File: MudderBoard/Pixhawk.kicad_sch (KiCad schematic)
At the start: 18 parts, among them U1 TPS566242DRLR, U2 LP38691DTX-3.3/NOPB

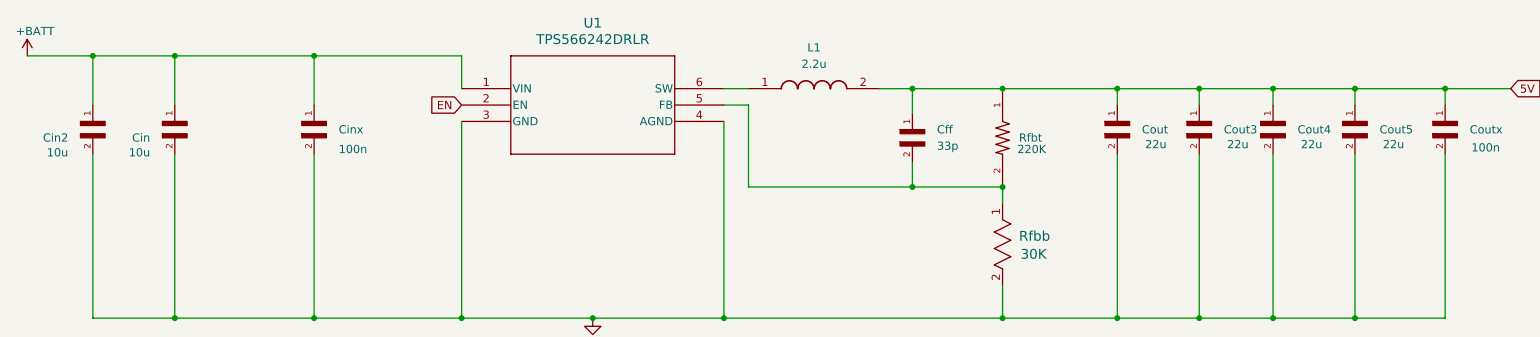
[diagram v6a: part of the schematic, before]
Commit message: Imported footprints to layout
Colin - Make note of these

C30,C32 are generic 0805 caps
L4,L5 are basic insuctors, will need to change when we figure this situation out!

U8,U9 changed to same boost IC as Lidar - these are the same right?
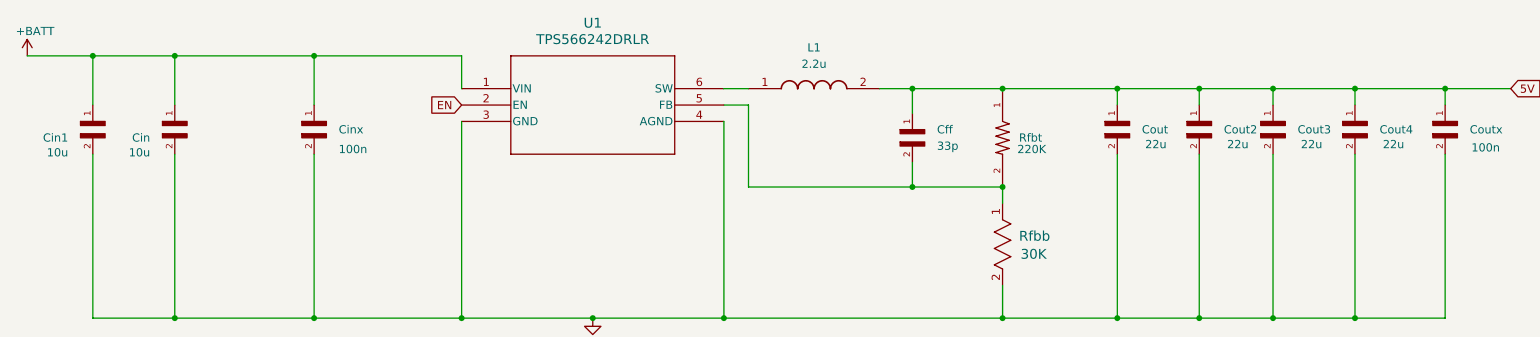
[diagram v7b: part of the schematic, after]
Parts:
- renumbered Cin2 to Cin1, Cout3 to Cout2, Cout4 to Cout3, Cout5 to Cout4
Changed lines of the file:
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@@
 			(project "MudderBoard"
 				(path "/cdf98bf7-80ce-4b13-b655-e6c7c589c122/0627c6a6-a63c-4c7b-88fc-6e03d8d4f91c"
-					(reference "L1")
+					(reference "L2")
 					(unit 1)
 				)
@@
 			(project "MudderBoard"
 				(path "/cdf98bf7-80ce-4b13-b655-e6c7c589c122/0627c6a6-a63c-4c7b-88fc-6e03d8d4f91c"
-					(reference "Cout2")
+					(reference "Cout1")
 					(unit 1)
 				)
@@
 		(on_board yes)
 		(dnp no)
-		(property "Reference" "Cout4"
+		(property "Reference" "Cout3"
 			(at 236.22 50.7999 90)
 			(effects
@@
 			(project "MudderBoard"
 				(path "/cdf98bf7-80ce-4b13-b655-e6c7c589c122/0627c6a6-a63c-4c7b-88fc-6e03d8d4f91c"
-					(reference "Cout4")
+					(reference "Cout3")
 					(unit 1)
 				)
@@
 			(project "MudderBoard"
 				(path "/cdf98bf7-80ce-4b13-b655-e6c7c589c122/0627c6a6-a63c-4c7b-88fc-6e03d8d4f91c"
-					(reference "Rfbb2")
+					(reference "Rfbb1")
 					(unit 1)
 				)
@@
 			(project "MudderBoard"
 				(path "/cdf98bf7-80ce-4b13-b655-e6c7c589c122/0627c6a6-a63c-4c7b-88fc-6e03d8d4f91c"
-					(reference "#PWR0104")
+					(reference "#PWR010")
 					(unit 1)
 				)
@@
 			(project "MudderBoard"
 				(path "/cdf98bf7-80ce-4b13-b655-e6c7c589c122/0627c6a6-a63c-4c7b-88fc-6e03d8d4f91c"
-					(reference "#PWR0101")
+					(reference "#PWR08")
 					(unit 1)
 				)
@@
 			(project "MudderBoard"
 				(path "/cdf98bf7-80ce-4b13-b655-e6c7c589c122/0627c6a6-a63c-4c7b-88fc-6e03d8d4f91c"
-					(reference "Cin3")
+					(reference "Cin2")
 					(unit 1)
 				)
@@
 			(project "MudderBoard"
 				(path "/cdf98bf7-80ce-4b13-b655-e6c7c589c122/0627c6a6-a63c-4c7b-88fc-6e03d8d4f91c"
-					(reference "U2")
+					(reference "U3")
 					(unit 1)
 				)
@@
 			(project "MudderBoard"
 				(path "/cdf98bf7-80ce-4b13-b655-e6c7c589c122/0627c6a6-a63c-4c7b-88fc-6e03d8d4f91c"
-					(reference "#PWR0103")
+					(reference "#PWR06")
 					(unit 1)
 				)
@@
 		(on_board yes)
 		(dnp no)
-		(property "Reference" "Cin2"
+		(property "Reference" "Cin1"
 			(at 45.72 52.0701 90)
 			(effects
@@
 			(project "MudderBoard"
 				(path "/cdf98bf7-80ce-4b13-b655-e6c7c589c122/0627c6a6-a63c-4c7b-88fc-6e03d8d4f91c"
-					(reference "Cin2")
+					(reference "Cin1")
 					(unit 1)
 				)
@@
 			(project "MudderBoard"
 				(path "/cdf98bf7-80ce-4b13-b655-e6c7c589c122/0627c6a6-a63c-4c7b-88fc-6e03d8d4f91c"
-					(reference "#PWR0102")
+					(reference "#PWR07")
 					(unit 1)
 				)
@@
 			(project "MudderBoard"
 				(path "/cdf98bf7-80ce-4b13-b655-e6c7c589c122/0627c6a6-a63c-4c7b-88fc-6e03d8d4f91c"
-					(reference "U1")
+					(reference "U2")
 					(unit 1)
 				)
@@
 		(on_board yes)
 		(dnp no)
-		(property "Reference" "Cout3"
+		(property "Reference" "Cout2"
 			(at 224.79 50.7999 90)
 			(effects
@@
 			(project "MudderBoard"
 				(path "/cdf98bf7-80ce-4b13-b655-e6c7c589c122/0627c6a6-a63c-4c7b-88fc-6e03d8d4f91c"
-					(reference "Cout3")
+					(reference "Cout2")
 					(unit 1)
 				)
@@
 		(on_board yes)
 		(dnp no)
-		(property "Reference" "Cout5"
+		(property "Reference" "Cout4"
 			(at 248.92 50.7999 90)
 			(effects
@@
 			(project "MudderBoard"
 				(path "/cdf98bf7-80ce-4b13-b655-e6c7c589c122/0627c6a6-a63c-4c7b-88fc-6e03d8d4f91c"
-					(reference "Cout5")
+					(reference "Cout4")
 					(unit 1)
 				)
@@
 			(project "MudderBoard"
 				(path "/cdf98bf7-80ce-4b13-b655-e6c7c589c122/0627c6a6-a63c-4c7b-88fc-6e03d8d4f91c"
-					(reference "#PWR0105")
-					(unit 1)
-				)
+					(reference "#PWR09")
+					(unit 1)
+				)

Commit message: PWM-DC prelim layout
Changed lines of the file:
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@@
+		)
+	)
+	(label "5V"
+		(at 269.24 44.45 0)
+		(fields_autoplaced yes)
+		(effects
+			(font
+				(size 1.27 1.27)
+			)
+			(justify left bottom)
 		)
 	)
@@
 				(hide yes)
 			)
-		)
-	)
-	(global_label "5V"
-		(shape input)
-		(at 269.24 44.45 0)
-		(fields_autoplaced yes)
-		(effects
-			(font
-				(size 1.27 1.27)
-			)
-			(justify left)
-		)
-		(property "Intersheetrefs" "${INTERSHEET_REFS}"
-			(at 274.5233 44.45 0)
-			(effects
-				(font
-					(size 1.27 1.27)
-				)
-				(justify left)
-				(hide yes)
-			)
